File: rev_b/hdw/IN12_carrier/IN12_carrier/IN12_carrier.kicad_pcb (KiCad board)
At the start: 4 copper layers, 200 x 50 mm, 200 parts, among them J1001 Cap SNS, J201 Conn_02x32_Top_Bottom, Q401 MMSTA42, Q402 MMSTA42, Q403 MMSTA42, Q404 MMSTA92, Q405 MMSTA92, Q406 MMSTA92, Q407 MMSTA42, Q408 MMSTA42, Q409 MMSTA42, Q410 MMSTA92, Q411 MMSTA92, Q412 MMSTA92, Q501 MMSTA42, Q502 MMSTA42, Q503 MMSTA42, Q504 MMSTA42, Q505 MMSTA42, Q506 MMSTA42, Q507 MMSTA42, Q508 MMSTA42, Q509 MMSTA42, Q510 MMSTA42, Q511 MMSTA42, Q512 MMSTA42, Q513 MMSTA42, Q514 MMSTA42, Q515 MMSTA42, U1001 TCA9555RGER, U1002 24AA02-OT, U1003 AT42QT1010-TSHR, U1004 AT42QT1010-TSHR, U1005 AT42QT1010-TSHR, U1006 AT42QT1010-TSHR, U1007 AT42QT1010-TSHR, U301 DS1683, U302 LTC4316DD, U701 LP5009, U702 LP5009, U703 LP5009

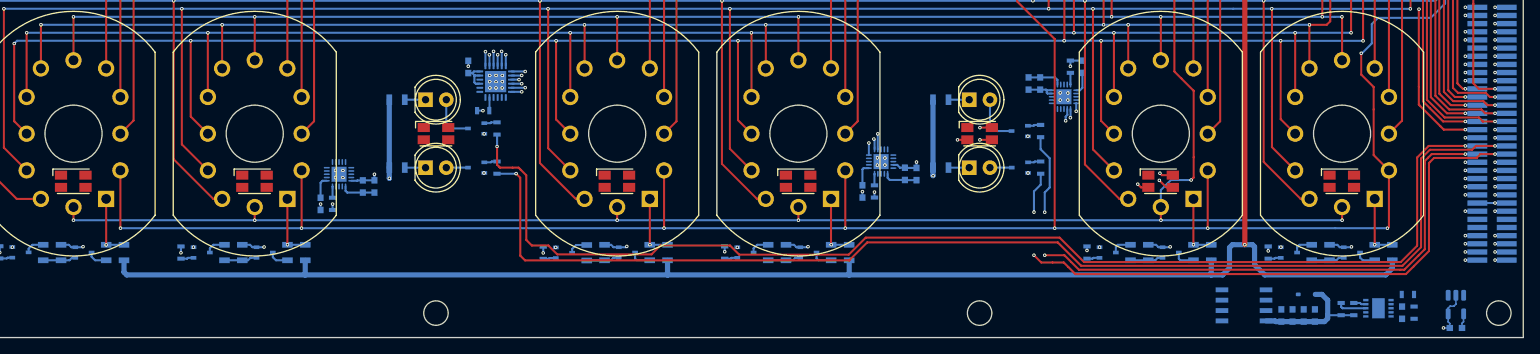
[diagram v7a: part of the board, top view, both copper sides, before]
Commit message: more small signal routing on IN12 carrier
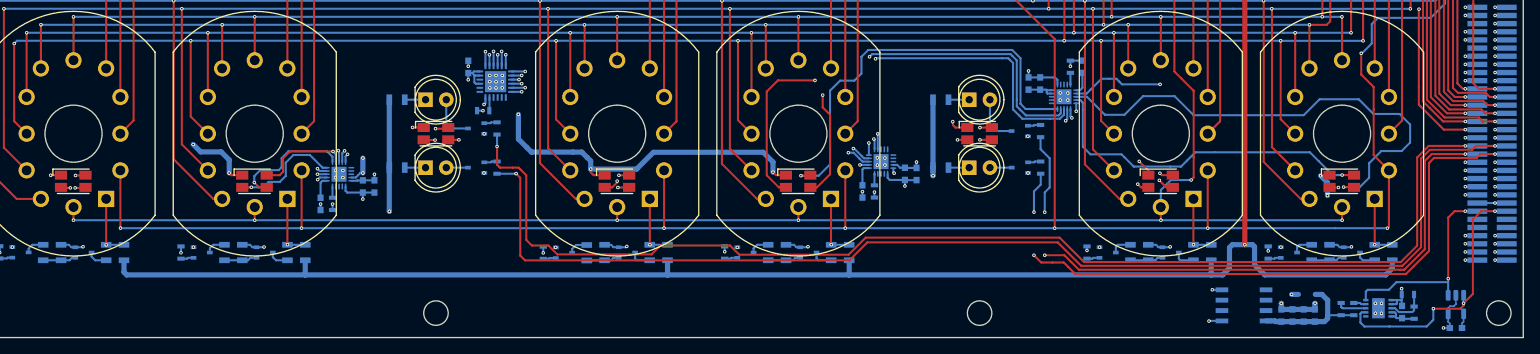
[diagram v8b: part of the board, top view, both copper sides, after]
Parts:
- moved C305 0.09 mm to (220.4, 129.2)
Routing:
- net COLON0_LED_R: track 0.00 -> 79.4 mm, vias 0 -> 2
- net +3.3V: track 43.2 -> 120.4 mm, vias 9 -> 30
- net COLON0_LED_B: track 0.00 -> 75.9 mm, vias 0 -> 2
- net COLON0_LED_G: track 0.00 -> 69.3 mm, vias 0 -> 2
- net TUBE2_LED_R: track 0.00 -> 61.9 mm, vias 0 -> 2
- net TUBE0_LED_G: track 0.00 -> 60.8 mm, vias 0 -> 1
- net TUBE2_LED_G: track 0.00 -> 52.2 mm, vias 0 -> 2
- net TUBE2_LED_B: track 0.00 -> 51.8 mm, vias 0 -> 1
- net TUBE3_LED_R: track 0.00 -> 51.0 mm, vias 0 -> 2
- net TUBE5_LED_R: track 0.00 -> 48.9 mm, vias 0 -> 2
- net TUBE3_LED_G: track 0.00 -> 44.1 mm, vias 0 -> 2
- net TUBE0_LED_R: track 0.00 -> 42.6 mm, vias 0 -> 2
- net TUBE0_LED_B: track 0.00 -> 42.5 mm, vias 0 -> 1
- net TUBE3_LED_B: track 0.00 -> 41.1 mm, vias 0 -> 2
- net TUBE5_LED_B: track 0.00 -> 40.5 mm, vias 0 -> 2
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- added copper zone on In1.Cu, net +3.3V
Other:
- board text added: "To-Do: * Fix I2C net naming * Enter stackup in design rules * Stackup legend * Owl * Board name * Board date * Board stats"
- board text removed: "To-Do: * Enter stackup in design rules * Stackup legend * Owl * Board name * Board date * Board stats"
